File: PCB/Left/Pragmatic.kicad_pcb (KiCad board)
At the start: 2 copper layers, 75 parts, among them J1 Conn_02x07_Odd_Even, SW1 SW_Push, SW10 SW_Push, SW11 SW_Push, SW12 SW_Push, SW13 SW_Push, SW14 SW_Push, SW15 SW_Push, SW16 SW_Push, SW17 SW_Push, SW18 SW_Push, SW19 SW_Push, SW2 SW_Push, SW20 SW_Push, SW21 SW_Push, SW22 SW_Push, SW23 SW_Push, SW24 SW_Push, SW25 SW_Push, SW26 SW_Push, SW27 SW_Push, SW28 SW_Push, SW29 SW_Push, SW3 SW_Push, SW30 SW_Push, SW31 SW_Push, SW32 SW_Push, SW33 SW_Push, SW34 SW_Push, SW35 SW_Push, SW36 SW_Push, SW4 SW_Push, SW5 SW_Push, SW6 SW_Push, SW7 SW_Push, SW8 SW_Push, SW9 SW_Push

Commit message: left ready
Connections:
- J1 pad 10: Col3 -> Col2
- J1 pad 11: Row4 -> Col3
- J1 pad 13: Col6 -> Col5
- J1 pad 14: Col5 -> Col6
- J1 pad 6: Col1 -> Row4
- J1 pad 7: Row6 -> Row5
- J1 pad 8: Col2 -> Row6
- J1 pad 9: Row5 -> Col1
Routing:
- net Col1: track 34.4 -> 176.2 mm
- net Col2: track 28.5 -> 154.6 mm
- net Row4: track 64.4 -> 163.7 mm, vias 0 -> 2
- net Row6: track 103.8 -> 201.7 mm
- net Row5: track 84.3 -> 179.9 mm, vias 0 -> 2
- net Row3: track 50.0 -> 142.6 mm, vias 0 -> 2
- net Net-(D37-Pad2): track 0.00 -> 17.5 mm
- net Col3: track 126.6 -> 141.9 mm
- net Net-(D32-Pad2): track 0.00 -> 13.5 mm
- net Net-(D28-Pad2): track 0.00 -> 13.5 mm
- net Net-(D26-Pad2): track 0.00 -> 13.5 mm
- net Net-(D25-Pad2): track 0.00 -> 13.5 mm
- net Net-(D34-Pad2): track 0.00 -> 13.5 mm
- net Net-(D31-Pad2): track 0.00 -> 13.5 mm
- net Net-(D16-Pad2): track 0.00 -> 13.5 mm
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
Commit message: left done
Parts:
- moved D37 3.07 mm to (88.2, 42.9), turned to 180 degrees
- moved R1 0.24 mm to (71.1, 42.9)
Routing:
- net VCC: track 14.0 -> 9.19 mm
- net Net-(D37-Pad2): track 17.5 -> 15.4 mm
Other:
- board outline added: 114.3 x 123.8 mm
- board text added: "Pragmatic"
- board text added: "v1 by James Sa 2021-11-07"

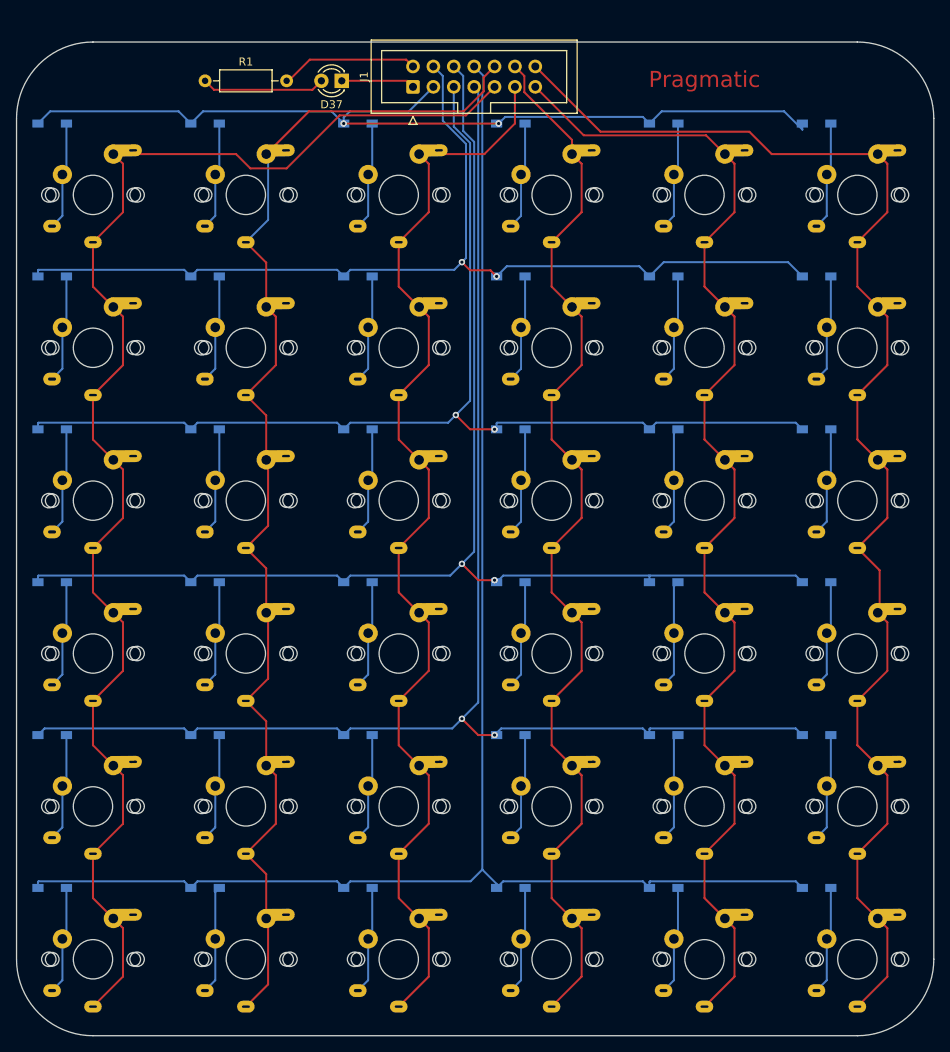
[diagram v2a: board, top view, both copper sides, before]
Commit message: fix power track width
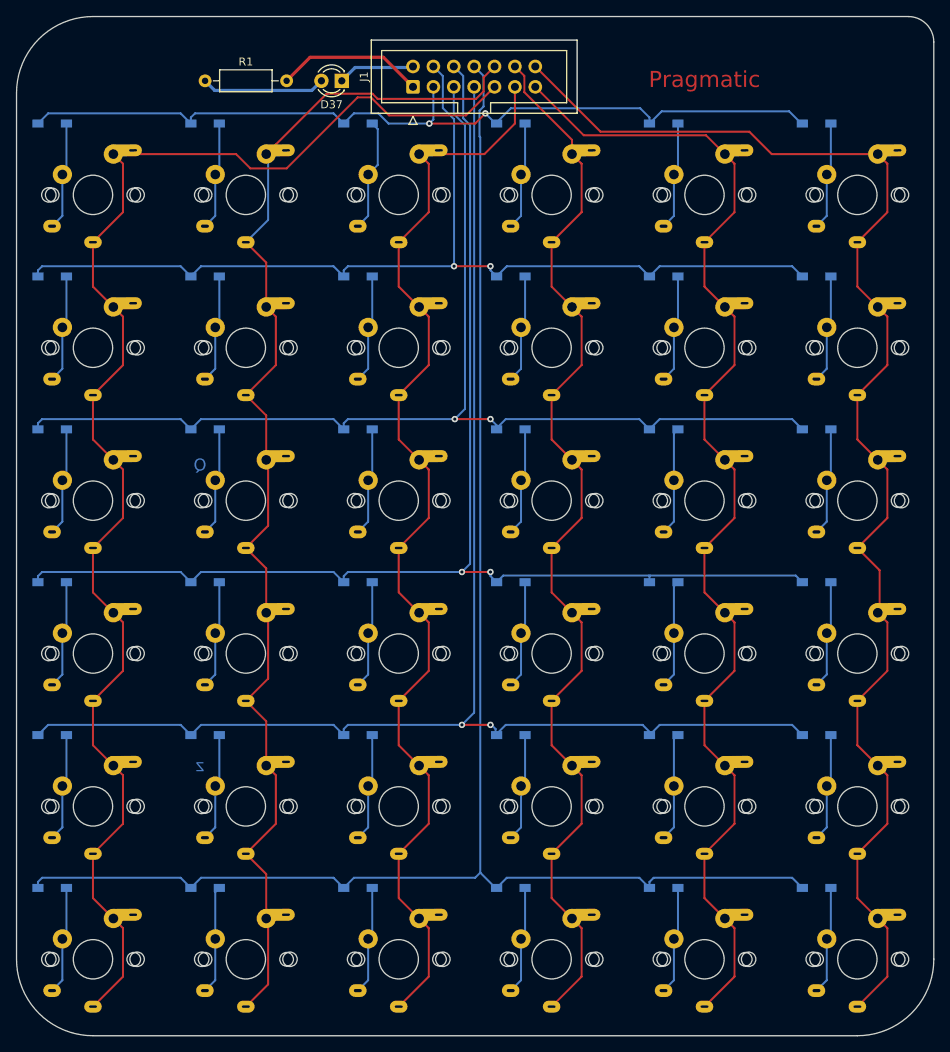
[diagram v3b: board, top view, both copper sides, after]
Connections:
- D37 pad 1: VCC -> Ground
- R1 pad 2: Ground -> VCC
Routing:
- net VCC: track 9.19 -> 18.5 mm
- net Ground: track 17.3 -> 9.61 mm
- net Row1: track 114.3 -> 108.0 mm
- net Col1: track 176.2 -> 178.1 mm
- net Row5: track 179.9 -> 181.7 mm
- net Row3: track 142.6 -> 144.3 mm
- net Row4: track 163.7 -> 165.3 mm
- net Row6: track 201.7 -> 203.1 mm
- net Net-(D3-Pad2): track 13.5 -> 14.1 mm
- net Col2: track 154.6 -> 155.1 mm
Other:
- board size 114.3 x 123.8 mm -> 114.3 x 127 mm
- net class Power added: clearance 0.2, trace_width 0.4, via_dia 0.8, via_drill 0.4
- board text added: "Q"
- board text added: "z"

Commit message: finish up left
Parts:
- moved J1 38.0 mm to (59.1, 42.5)
- moved R1 20.4 mm to (91.4, 41.3)
- moved D37 2.46 mm to (85.7, 42.5), turned to 90 degrees
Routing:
- net Col5: track 150.9 -> 189.3 mm
- net Col6: track 171.2 -> 209.6 mm
- net Col1: track 178.1 -> 139.7 mm
- net Col4: track 137.6 -> 175.0 mm
- net VCC: track 18.5 -> 46.3 mm
- net Ground: track 9.61 -> 28.8 mm
- net Col2: track 155.1 -> 140.9 mm
- net Col3: track 141.9 -> 154.5 mm
- net Net-(D37-Pad2): track 15.5 -> 6.24 mm
- net Row1: track 108.0 -> 106.1 mm
- net Row6: track 203.1 -> 204.9 mm
- net Row5: track 181.7 -> 183.2 mm
- net Row4: track 165.3 -> 166.7 mm
- net Row2: track 127.6 -> 128.7 mm
- net Row3: track 144.3 -> 144.8 mm
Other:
- outline, holes or cut-outs redrawn
- board text added: "Left side"
- board text added: "Pragmatic Kit Design by James Sa V0.1 2021-11-8"
- board text removed: "v1 by James Sa 2021-11-07"

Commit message: finish up
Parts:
- added REF**: Logo, Pragmatic:Logo, F.Cu at (133.3, 41.3)
- moved D37 2.84 mm to (83.2, 41.3), turned to 0 degrees
- moved R1 1.27 mm to (90.2, 41.3)
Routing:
- net Ground: track 28.8 -> 25.7 mm
- net Net-(D37-Pad2): track 6.24 -> 4.45 mm
- net VCC: track 46.3 -> 48.0 mm
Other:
- board text added: "Bernard"
- board text added: "Pragmatic Kit Left Hand Module Design by James Sa V0.1 2021-11-8"
- board text removed: "Pragmatic"
- board text removed: "Pragmatic Kit Design by James Sa V0.1 2021-11-8"
